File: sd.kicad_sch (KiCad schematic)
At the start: 47 parts, among them J3 Micro_SD_Card, J4 uSD_edge_contacts, Q1 DMG1032UV, Q2 DMG1013UW, Q3 DMG1032UV, U11 SN74LVC1G14DRL, U12 TS3DDR4000ZBAR, U13 74AUC1G86, U14 GL3224-OIYxx, U15 25LCxxx-MC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

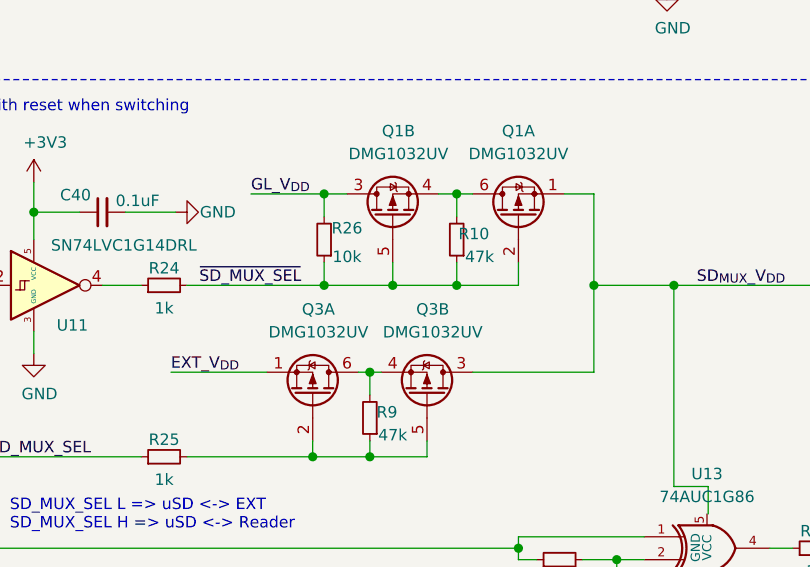
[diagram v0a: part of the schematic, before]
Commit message: SDReWire: fix back-to-back transistors circuit
Signed-off-by: Dominik Sliwa <dominik@sliwa.io>
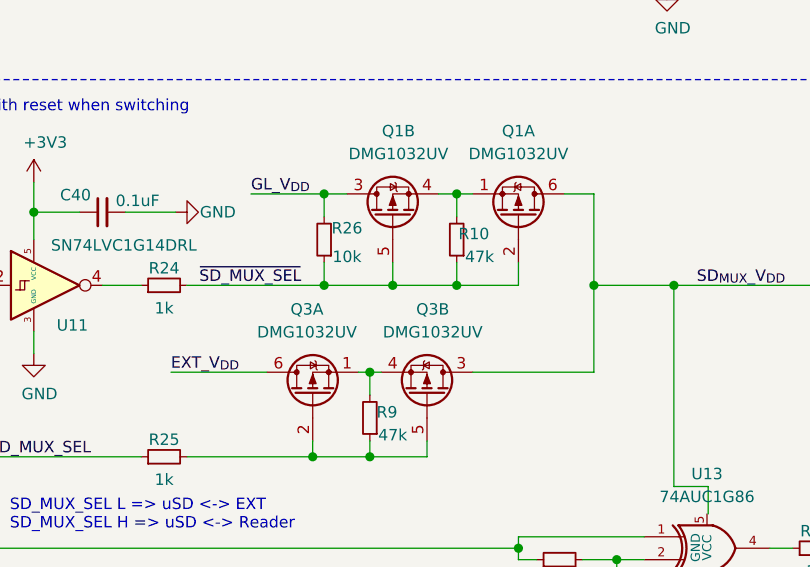
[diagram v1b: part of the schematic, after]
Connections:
- net EXT_V_{DD}: now also Q3.6 (D); no longer Q3.1 (S)
- net SD_{MUX}_V_{DD}: now also Q1.6 (D); no longer Q1.1 (S)
- net at Q1.4 (S), R10.2: now also Q1.1 (S); no longer Q1.6 (D)
- net at Q3.4 (S), R9.2: now also Q3.1 (S); no longer Q3.6 (D)
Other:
- moved on the sheet: Q1A, Q3A
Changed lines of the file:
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@@
   (junction (at 247.142 42.672) (diameter 1.016) (color 0 0 0 0))
   (junction (at 257.81 95.25) (diameter 1.016) (color 0 0 0 0))
+  (no_connect (at 125.73 105.41))
+  (no_connect (at 125.73 52.07))
+  (no_connect (at 125.73 62.23))
+  (no_connect (at 125.73 80.01))
   (no_connect (at 125.73 90.17))
+  (no_connect (at 125.73 100.33))
+  (no_connect (at 125.73 57.15))
+  (no_connect (at 125.73 85.09))
+  (no_connect (at 125.73 72.39))
+  (no_connect (at 95.25 72.39))
+  (no_connect (at 95.25 57.15))
   (no_connect (at 95.25 52.07))
-  (no_connect (at 125.73 72.39))
-  (no_connect (at 125.73 52.07))
+  (no_connect (at 27.94 44.45))
+  (no_connect (at 125.73 67.31))
+  (no_connect (at 125.73 95.25))
+  (no_connect (at 95.25 62.23))
+  (no_connect (at 95.25 46.99))
   (no_connect (at 125.73 46.99))
   (no_connect (at 95.25 67.31))
-  (no_connect (at 95.25 62.23))
-  (no_connect (at 95.25 72.39))
-  (no_connect (at 95.25 46.99))
-  (no_connect (at 95.25 57.15))
-  (no_connect (at 125.73 85.09))
-  (no_connect (at 27.94 44.45))
-  (no_connect (at 125.73 57.15))
-  (no_connect (at 125.73 95.25))
-  (no_connect (at 125.73 105.41))
-  (no_connect (at 125.73 80.01))
-  (no_connect (at 125.73 67.31))
-  (no_connect (at 125.73 100.33))
-  (no_connect (at 125.73 62.23))
   (wire (pts (xy 21.082 187.96) (xy 33.782 187.96))
     (stroke (width 0) (type solid) (color 0 0 0 0))
@@
     )
   )
-  (symbol (lib_id "Device:Q_Dual_PMOS_S1G1D2S2G2D1") (at 71.12 159.512 270) (mirror x) (unit 1)
-    (in_bom yes) (on_board yes)
-    (property "Reference" "Q3" (id 0) (at 71.755 149.987 90))
-    (property "Value" "DMG1032UV" (id 1) (at 71.755 152.527 90))
+  (symbol (lib_id "Device:Q_Dual_PMOS_S1G1D2S2G2D1") (at 71.12 159.512 90) (unit 1)
+    (in_bom yes) (on_board yes)
+    (property "Reference" "Q3" (id 0) (at 70.485 149.987 90))
+    (property "Value" "DMG1032UV" (id 1) (at 70.485 152.527 90))
     (property "Footprint" "Package_TO_SOT_SMD:SOT-563" (id 2) (at 71.12 158.242 0)
       (effects (font (size 1.27 1.27)) hide)
@@
     )
   )
-  (symbol (lib_id "Device:Q_Dual_PMOS_S1G1D2S2G2D1") (at 93.98 139.7 90) (unit 1)
+  (symbol (lib_id "Device:Q_Dual_PMOS_S1G1D2S2G2D1") (at 93.98 139.7 270) (mirror x) (unit 1)
     (in_bom yes) (on_board yes)
     (property "Reference" "Q1" (id 0) (at 93.98 130.175 90))

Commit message: Changes:
-fix led order
-fix transistor routing
-modify usb hub strapping and fix crystal footprint
-remove copper under sd pads
-routing cleanup
-change revision to 1.1

Signed-off-by: Dominik Sliwa <dominik@sliwa.io>
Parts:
- removed R11: DNI, Resistor_SMD:R_0402_1005Metric, symbol Device:R_Small
- C19, C20: value 6pF -> 22pF
- C44: value 4.7uF -> 0.1uF
- C48: footprint Capacitor_SMD:C_0201_0603Metric -> Capacitor_SMD:C_0402_1005Metric
- Q1, Q3: value DMG1032UV -> DMG1023UV
- R10, R9: value 47k -> 100k
- R37: value 4k7 -> 1k
- R39: value 4k7 -> 10k
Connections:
- net +3V3: now also RN1.6 (R3.2); no longer RN1.5 (R4.2)
- net GL_V_{DD}: no longer R26.2
- net SD_{MUX}_V_{DD}: now also R26.2
- net ~SD_MUX_SEL: now also RN1.5 (R4.2); no longer RN1.6 (R3.2)
- net at RN1.4 (R4.1): now also D4.2 (A); no longer D3.2 (A)
- net at RN1.3 (R3.1): now also D3.2 (A); no longer D4.2 (A)
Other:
- company: (none) -> SliwaIO
- title: (none) -> SDReWire
- moved on the sheet: R26, RN1C, RN1D
